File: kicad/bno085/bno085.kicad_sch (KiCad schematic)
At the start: 39 parts, among them J1 USB4125-GF-A_REVA, J2 Conn_02x03_Odd_Even, J3 Conn_01x05, J4 Conn_01x02, SW1 SW_SPDT, U1 MCP73832-2-OT, U2 BQ297xy, U3 CSD85302L, U4 NCP177BMX330TCG, U5 ASAK-32.7680KHZ-LRS-T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

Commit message: added Datasheets and updated shimatics for bno085 board
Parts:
- U2: value BQ297xy -> BQ29701DSET
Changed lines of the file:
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@@
     (in_bom yes) (on_board yes)
     (property "Reference" "U2" (id 0) (at 58.42 128.27 0))
-    (property "Value" "BQ297xy" (id 1) (at 57.15 142.24 0))
+    (property "Value" "BQ29701DSET" (id 1) (at 59.69 142.24 0))
     (property "Footprint" "Package_SON:WSON-6_1.5x1.5mm_P0.5mm" (id 2) (at 52.07 125.73 0)
       (effects (font (size 1.27 1.27)) hide)
@@
     )
     (path "/00000000-0000-0000-0000-000060e4ae03"
-      (reference "U2") (unit 1) (value "BQ297xy") (footprint "Package_SON:WSON-6_1.5x1.5mm_P0.5mm")
+      (reference "U2") (unit 1) (value "BQ29701DSET") (footprint "Package_SON:WSON-6_1.5x1.5mm_P0.5mm")
     )
     (path "/00000000-0000-0000-0000-000060e548a0"

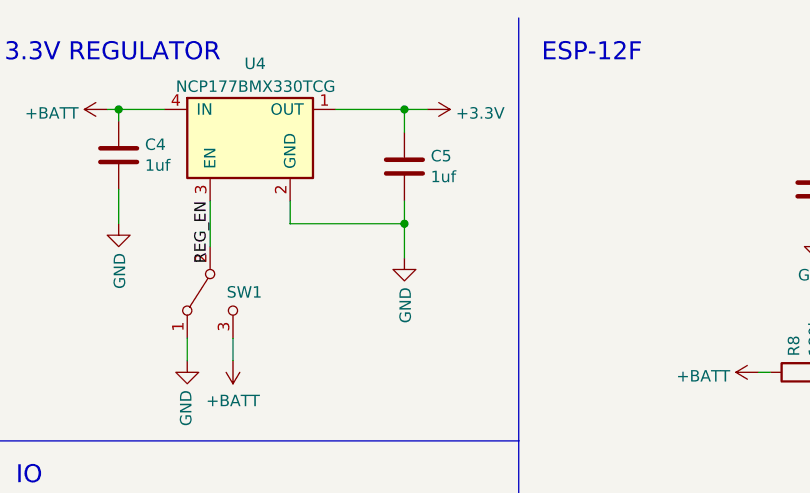
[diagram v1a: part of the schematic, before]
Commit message: made minor cahnges to bno085 schimatic + pcb to better reflect the real world version
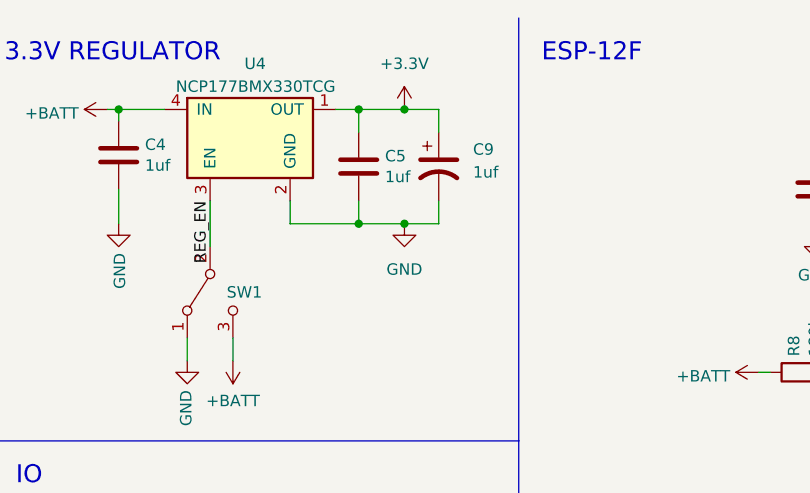
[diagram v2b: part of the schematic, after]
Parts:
- added C9: 1uf, symbol Device:C_Polarized_US
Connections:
- net +3.3V: now also C9.1
- net GND: now also C9.2
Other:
- moved on the sheet: C5
